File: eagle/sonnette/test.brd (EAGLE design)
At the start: 155.9 x 100.3 mm, 14 parts, among them IC1 7805TV, IC2 4066N, Q1 60V/32A/35mΩ

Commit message: update schema for receiver
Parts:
- added C3: 33uF, SparkFun-Capacitors:CAP-PTH-SMALL-KIT
- added C4: 0.47uF, SparkFun-Capacitors:CAP-PTH-SMALL-KIT
- added C5, C6, C7: 10uF, SparkFun-Capacitors:CPOL-RADIAL-2.5MM-5MM
- added FM_TX, JP7: (no value), pinhead:1X04
- added IC3: LM3840, linear:TO220V
- added J1: POWER_JACK, SparkFun-Connectors:POWER_JACK_PTH
- added JP3, JP4: (no value), pinhead:1X05
- added JP5, JP6: (no value), pinhead:1X06
- added JP8: (no value), pinhead:1X02
- added LCD1: LCD-16X2SILK, SparkFun-Displays:LCD-16X2
- added LS1: SPEAKER, SparkFun-Electromechanical:PCB_MOUNT_SPEAKER
- added Q2: IRFZ44N, SparkFun-DiscreteSemi:TO220V
- added R10, R12, R13, R5: 4.7k, SparkFun-Resistors:AXIAL-0.3
- added R11, R14, R6, R9: 1k, SparkFun-Resistors:AXIAL-0.3
- added R15: (no value), rcl:PT-10
- added R3, R4, R7, R8: 10k, SparkFun-Resistors:AXIAL-0.3
- added S1: (no value), SparkFun-Switches:TACTILE_SWITCH_PTH_6.0MM
- added T1: 2N2222, adafruit:TO92-EBC-OVAL
- Q1: value 60V/32A/35mΩ -> IRFZ44N
- moved IC2 59.7 mm to (-71.1, -208.3)
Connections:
- removed net VDD: IC2.14
- removed net VSS: IC2.7
- new net 3V3_REGU: C3.1, IC3.3, JP3.1, JP6.4
- new net 5V_ON: Q2.1, R6.P$2
- new net 5V_REGU: C4.1, FM_TX.2, IC3.1, JP5.4, Q2.3, R8.P$1
- new net AUDIO_OUT1: JP4.2, JP4.3
- new net AUDIO_OUT2: C5.2, C7.2, U$1.D12
- new net AUDIO_SELECT: IC2.6, R7.P$2, U$1.D13
- new net E: LCD1.6, U$1.D9
- new net N$10: R5.P$1, U$2.ANT, U$2.DATA
- new net N$11: JP3.5, JP6.6
- new net N$12: JP3.4, JP6.5
- new net N$13: R7.P$1, T1.B
- new net N$14: IC2.8, R10.P$2
- new net N$15: C5.1, R10.P$1, R9.P$1
- new net N$16: IC2.5, R8.P$2, T1.C
- new net N$17: IC2.4, R12.P$2
- new net N$18: C7.1, R11.P$1, R12.P$1
- new net N$19: JP8.1, LS1.+
- new net N$20: JP7.3, JP7.4
- new net N$21: C6.2, IC2.3, IC2.9, R13.P$2
- new net N$22: C6.1, JP7.2
- new net N$23: R13.P$1
- new net N$24: JP8.2, LS1.-
- new net N$25: J1.GND, J1.GNDBREAK
- new net N$26: S1.3, U$1.D5
- new net N$27: LCD1.14, U$1.A0
- new net N$28: LCD1.13, U$1.A1
- new net N$29: LCD1.12, U$1.A2
- new net N$30: LCD1.11, U$1.A3
- new net N$31: LCD1.2
- new net N$32: LCD1.1, R15.2
- new net N$34: LCD1.15, R14.P$2
- new net N$36: LCD1.3, R15.3
- new net N$8: IC2.13, R4.P$1
- new net N$9: IC2.2, R5.P$2
- new net RS: LCD1.4, U$1.D8
- new net SCL: FM_TX.4, JP5.5, U$1.A5
- new net SDA: FM_TX.3, JP5.6, U$1.A4
- net 12V: now also IC2.14, JP7.1, R3.P$2; no longer IC2.1
- net GND: now also C3.2, C4.2, DC1.13, DC1.15, FM_TX.1, IC2.7, IC3.2, JP4.1, JP5.3, JP6.3, LCD1.16, R11.P$2, T1.E
- net N$6: now also J1.PWR
- net N$7: now also DC1.24, Q1.3; no longer DC1.13, Q1.2
- net RF_TX: now also R4.P$2, U$1.D7; no longer IC2.13, IC2.2, U$1.D8, U$2.ANT, U$2.DATA
- net VCC: now also Q1.2, Q2.2, R14.P$1, R15.1; no longer DC1.24

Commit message: update
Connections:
- removed net N$13: R7.P$1, T1.B
- net AUDIO_SELECT: now also R7.P$1, T1.B
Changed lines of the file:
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@@
 <wire x1="67.31" y1="52.07" x2="-76.18" y2="-505.46" width="0" layer="19" extent="1-1"/>
-</signal>
-<signal name="N$13">
-<contactref element="R7" pad="P$1"/>
-<contactref element="T1" pad="B"/>
-<wire x1="-76.2" y1="-452.12" x2="-74.93" y2="-468.63" width="0" layer="19" extent="1-1"/>
 </signal>
 <signal name="AUDIO_SELECT">
 <contactref element="U$1" pad="D13"/>
+<contactref element="IC2" pad="6"/>
+<contactref element="R7" pad="P$1"/>
+<contactref element="T1" pad="B"/>
 <contactref element="R7" pad="P$2"/>
-<contactref element="IC2" pad="6"/>
 <wire x1="-66.04" y1="-212.09" x2="64.77" y2="52.07" width="0" layer="19" extent="1-1"/>
-<wire x1="-67.31" y1="-468.63" x2="-66.04" y2="-212.09" width="0" layer="19" extent="1-1"/>
+<wire x1="-76.2" y1="-452.12" x2="-66.04" y2="-212.09" width="0" layer="19" extent="1-1"/>
+<wire x1="-74.93" y1="-468.63" x2="-76.2" y2="-452.12" width="0" layer="19" extent="1-1"/>
+<wire x1="-67.31" y1="-468.63" x2="-74.93" y2="-468.63" width="0" layer="19" extent="1-1"/>
 </signal>
 <signal name="N$16">

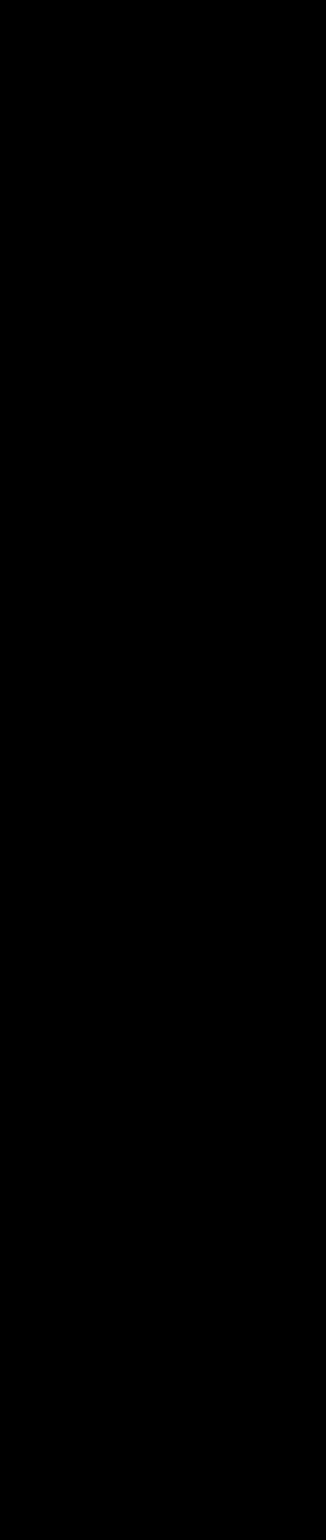
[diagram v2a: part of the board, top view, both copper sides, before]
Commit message: updated eagle schema
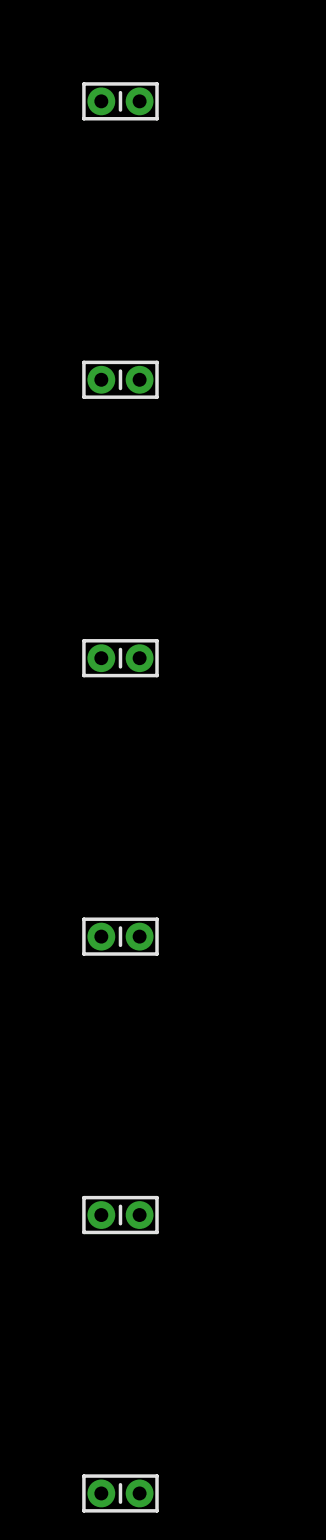
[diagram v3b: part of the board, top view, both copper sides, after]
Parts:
- added C10, C11, C12, C13, C8, C9: 0.1uF, SparkFun-Capacitors:CAP-PTH-SMALL-KIT
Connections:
- new net N$13: R6.P$1, U$1.D11
- net 12V: now also C13.1, C8.1
- net 3V3_REGU: now also C10.2
- net 5V_REGU: now also C11.2
- net AUDIO_OUT1: now also C7.2
- net AUDIO_OUT2: no longer C7.2
- net GND: now also C10.1, C11.1, C12.2, C13.2, C8.2, J1.GND, J1.GNDBREAK, LCD1.5, R9.P$2, S1.1
- net N$25: now also IC2.1, R3.P$1; no longer J1.GND, J1.GNDBREAK
- net VCC: now also C12.1
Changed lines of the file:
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@@
 </element>
 <element name="R15" library="rcl" package="PT-10" value="" x="-144.78" y="-795.02"/>
+<element name="C8" library="SparkFun-Capacitors" package="CAP-PTH-SMALL-KIT" value="0.1uF" x="-143.51" y="-820.42">
+<attribute name="PROD_ID" value="CAP-08370" x="-143.51" y="-820.42" size="1.778" layer="27" display="off"/>
+</element>
+<element name="C9" library="SparkFun-Capacitors" package="CAP-PTH-SMALL-KIT" value="0.1uF" x="-143.51" y="-840.74">
+<attribute name="PROD_ID" value="CAP-08370" x="-143.51" y="-840.74" size="1.778" layer="27" display="off"/>
+</element>
+<element name="C10" library="SparkFun-Capacitors" package="CAP-PTH-SMALL-KIT" value="0.1uF" x="-143.51" y="-861.06">
+<attribute name="PROD_ID" value="CAP-08370" x="-143.51" y="-861.06" size="1.778" layer="27" display="off"/>
+</element>
+<element name="C11" library="SparkFun-Capacitors" package="CAP-PTH-SMALL-KIT" value="0.1uF" x="-143.51" y="-881.38">
+<attribute name="PROD_ID" value="CAP-08370" x="-143.51" y="-881.38" size="1.778" layer="27" display="off"/>
+</element>
+<element name="C12" library="SparkFun-Capacitors" package="CAP-PTH-SMALL-KIT" value="0.1uF" x="-143.51" y="-901.7">
+<attribute name="PROD_ID" value="CAP-08370" x="-143.51" y="-901.7" size="1.778" layer="27" display="off"/>
+</element>
+<element name="C13" library="SparkFun-Capacitors" package="CAP-PTH-SMALL-KIT" value="0.1uF" x="-143.51" y="-922.02">
+<attribute name="PROD_ID" value="CAP-08370" x="-143.51" y="-922.02" size="1.778" layer="27" display="off"/>
+</element>
 </elements>
 <signals>
@@
 <contactref element="C1" pad="1"/>
 <contactref element="U$3" pad="VCC"/>
-<contactref element="Q1" pad="2"/>
-<contactref element="Q2" pad="2"/>
 <contactref element="R14" pad="P$1"/>
 <contactref element="R15" pad="1"/>
+<contactref element="C12" pad="1"/>
+<contactref element="Q2" pad="2"/>
+<contactref element="Q1" pad="2"/>
 <wire x1="-44.577" y1="-91.44" x2="-74.93" y2="-129.54" width="0" layer="19" extent="1-1"/>
 <wire x1="-69.85" y1="-187.833" x2="-74.93" y2="-129.54" width="0" layer="19" extent="1-1"/>
@@
 <wire x1="-123.19" y1="-800.1" x2="-74.93" y2="-320.04" width="0" layer="19" extent="1-1"/>
 <wire x1="-147.32" y1="-800.1" x2="-123.19" y2="-800.1" width="0" layer="19" extent="1-1"/>
+<wire x1="-144.907" y1="-901.7" x2="-147.32" y2="-800.1" width="0" layer="19" extent="1-1"/>
 </signal>
 <signal name="GND">
@@
 <contactref element="R11" pad="P$2"/>
 <contactref element="LCD1" pad="16"/>
-<wire x1="-72.39" y1="-436.88" x2="-72.39" y2="-421.64" width="0" layer="19" extent="1-1"/>
+<contactref element="S1" pad="1"/>
+<contactref element="LCD1" pad="5"/>
+<contactref element="C12" pad="2"/>
+<contactref element="C11" pad="1"/>
+<contactref element="C13" pad="2"/>
+<contactref element="C10" pad="1"/>
+<contactref element="J1" pad="GNDBREAK"/>
+<contactref element="J1" pad="GND"/>
+<contactref element="R9" pad="P$2"/>
+<contactref element="C8" pad="2"/>
+<wire x1="-144.907" y1="-881.38" x2="-144.907" y2="-861.06" width="0" layer="19" extent="1-1"/>
+<wire x1="-142.113" y1="-901.7" x2="-144.907" y2="-881.38" width="0" layer="19" extent="1-1"/>
+<wire x1="-142.113" y1="-922.02" x2="-142.113" y2="-901.7" width="0" layer="19" extent="1-1"/>
+<wire x1="-142.113" y1="-820.42" x2="-144.907" y2="-861.06" width="0" layer="19" extent="1-1"/>
+<wire x1="-113.28" y1="-754.12" x2="-142.113" y2="-820.42" width="0" layer="19" extent="1-1"/>
+<wire x1="-123.9012" y1="-730.5294" x2="-113.28" y2="-754.12" width="0" layer="19" extent="1-1"/>
+<wire x1="-85.34" y1="-754.12" x2="-113.28" y2="-754.12" width="0" layer="19" extent="1-1"/>
+<wire x1="-111.76" y1="-698.42" x2="-123.9012" y2="-730.5294" width="0" layer="19" extent="1-1"/>
+<wire x1="-107.06" y1="-695.42" x2="-111.76" y2="-698.42" width="0" layer="19" extent="1-1"/>
+<wire x1="-67.31" y1="-577.85" x2="-107.06" y2="-695.42" width="0" layer="19" extent="1-1"/>
+<wire x1="-67.31" y1="-539.75" x2="-67.31" y2="-577.85" width="0" layer="19" extent="1-1"/>
+<wire x1="-78.74" y1="-452.12" x2="-67.31" y2="-539.75" width="0" layer="19" extent="1-1"/>
+<wire x1="-72.39" y1="-436.88" x2="-78.74" y2="-452.12" width="0" layer="19" extent="1-1"/>
+<wire x1="-72.39" y1="-421.64" x2="-72.39" y2="-436.88" width="0" layer="19" extent="1-1"/>
 <wire x1="-74.93" y1="-406.4" x2="-72.39" y2="-421.64" width="0" layer="19" extent="1-1"/>
-<wire x1="-78.74" y1="-452.12" x2="-72.39" y2="-436.88" width="0" layer="19" extent="1-1"/>
 <wire x1="-72.263" y1="-388.62" x2="-74.93" y2="-406.4" width="0" layer="19" extent="1-1"/>
 <wire x1="-72.263" y1="-368.3" x2="-72.263" y2="-388.62" width="0" layer="19" extent="1-1"/>
@@
 <wire x1="87.63" y1="75.057" x2="46.99" y2="52.07" width="0" layer="19" extent="1-1"/>
 <wire x1="92.71" y1="34.29" x2="87.63" y2="75.057" width="0" layer="19" extent="1-1"/>
-<wire x1="-67.31" y1="-577.85" x2="-78.74" y2="-452.12" width="0" layer="19" extent="1-1"/>
-<wire x1="-85.34" y1="-754.12" x2="-67.31" y2="-577.85" width="0" layer="19" extent="1-1"/>
 </signal>
 <signal name="N$2">
@@
 <contactref element="R3" pad="P$2"/>
 <contactref element="JP7" pad="1"/>
+<contactref element="C13" pad="1"/>
+<contactref element="C8" pad="1"/>
+<wire x1="-144.907" y1="-922.02" x2="-144.907" y2="-820.42" width="0" layer="19" extent="1-1"/>
+<wire x1="-77.47" y1="-631.19" x2="-144.907" y2="-820.42" width="0" layer="19" extent="1-1"/>
 <wire x1="-67.31" y1="-228.6" x2="-77.47" y2="-631.19" width="0" layer="19" extent="1-1"/>
 <wire x1="-78.74" y1="-204.47" x2="-67.31" y2="-228.6" width="0" layer="19" extent="1-1"/>
@@
 <contactref element="JP5" pad="4"/>
 <contactref element="R8" pad="P$1"/>
+<contactref element="C11" pad="2"/>
 <wire x1="-77.47" y1="-406.4" x2="-69.85" y2="-421.64" width="0" layer="19" extent="1-1"/>
 <wire x1="-75.057" y1="-388.62" x2="-77.47" y2="-406.4" width="0" layer="19" extent="1-1"/>
@@
 <wire x1="-72.39" y1="-320.04" x2="-75.057" y2="-388.62" width="0" layer="19" extent="1-1"/>
 <wire x1="-74.93" y1="-284.48" x2="-72.39" y2="-320.04" width="0" layer="19" extent="1-1"/>
+<wire x1="-142.113" y1="-881.38" x2="-74.93" y2="-487.68" width="0" layer="19" extent="1-1"/>
 </signal>
 <signal name="N$7">
@@
 <contactref element="JP6" pad="4"/>
 <contactref element="JP3" pad="1"/>
+<contactref element="C10" pad="2"/>
 <wire x1="-72.39" y1="-406.4" x2="-69.85" y2="-436.88" width="0" layer="19" extent="1-1"/>
 <wire x1="-75.057" y1="-368.3" x2="-72.39" y2="-406.4" width="0" layer="19" extent="1-1"/>
 <wire x1="-77.47" y1="-335.28" x2="-75.057" y2="-368.3" width="0" layer="19" extent="1-1"/>
+<wire x1="-142.113" y1="-861.06" x2="-69.85" y2="-436.88" width="0" layer="19" extent="1-1"/>
 </signal>
 <signal name="N$11">
@@
 <contactref element="JP4" pad="2"/>
 <contactref element="JP4" pad="3"/>
+<contactref element="C7" pad="2"/>
+<wire x1="-74.93" y1="-350.52" x2="-76.18" y2="-614.68" width="0" layer="19" extent="1-1"/>
 <wire x1="-72.39" y1="-350.52" x2="-74.93" y2="-350.52" width="0" layer="19" extent="1-1"/>
 </signal>
@@
 <contactref element="U$1" pad="D12"/>
 <contactref element="C5" pad="2"/>
-<contactref element="C7" pad="2"/>
-<wire x1="-76.18" y1="-505.46" x2="-76.18" y2="-614.68" width="0" layer="19" extent="1-1"/>
-<wire x1="67.31" y1="52.07" x2="-76.18" y2="-505.46" width="0" layer="19" extent="1-1"/>
+<wire x1="-76.18" y1="-505.46" x2="67.31" y2="52.07" width="0" layer="19" extent="1-1"/>
 </signal>
 <signal name="AUDIO_SELECT">
@@
 <wire x1="-60.96" y1="-706.12" x2="-74.93" y2="-646.43" width="0" layer="19" extent="1-1"/>
 </signal>
-<signal name="N$25">
-<contactref element="J1" pad="GNDBREAK"/>
-<contactref element="J1" pad="GND"/>
-<wire x1="-107.06" y1="-695.42" x2="-111.76" y2="-698.42" width="0" layer="19" extent="1-1"/>
-</signal>
 <signal name="N$26">
 <contactref element="U$1" pad="D5"/>
@@
 <wire x1="-118.36" y1="-754.12" x2="-144.78" y2="-789.94" width="0" layer="19" extent="1-1"/>
 </signal>
+<signal name="N$13">
+<contactref element="R6" pad="P$1"/>
+<contactref element="U$1" pad="D11"/>
+<wire x1="69.85" y1="52.07" x2="-74.93" y2="-302.26" width="0" layer="19" extent="1-1"/>
+</signal>
+<signal name="N$25">
+<contactref element="R3" pad="P$1"/>
+<contactref element="IC2" pad="1"/>
+<wire x1="-78.74" y1="-212.09" x2="-74.93" y2="-228.6" width="0" layer="19" extent="1-1"/>
+</signal>
 </signals>
